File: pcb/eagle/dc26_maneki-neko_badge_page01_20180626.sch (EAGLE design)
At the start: 55 parts, among them T1 RK7002BMT116, U1 STM32F030C8T, U2 PAM2301CAAB330, U3 NPTC042KFMS-RC, U4 MIC2005A-1YM5-TR, U5 MIC2005A-1YM5-TR, U6 MIC2005A-1YM5-TR

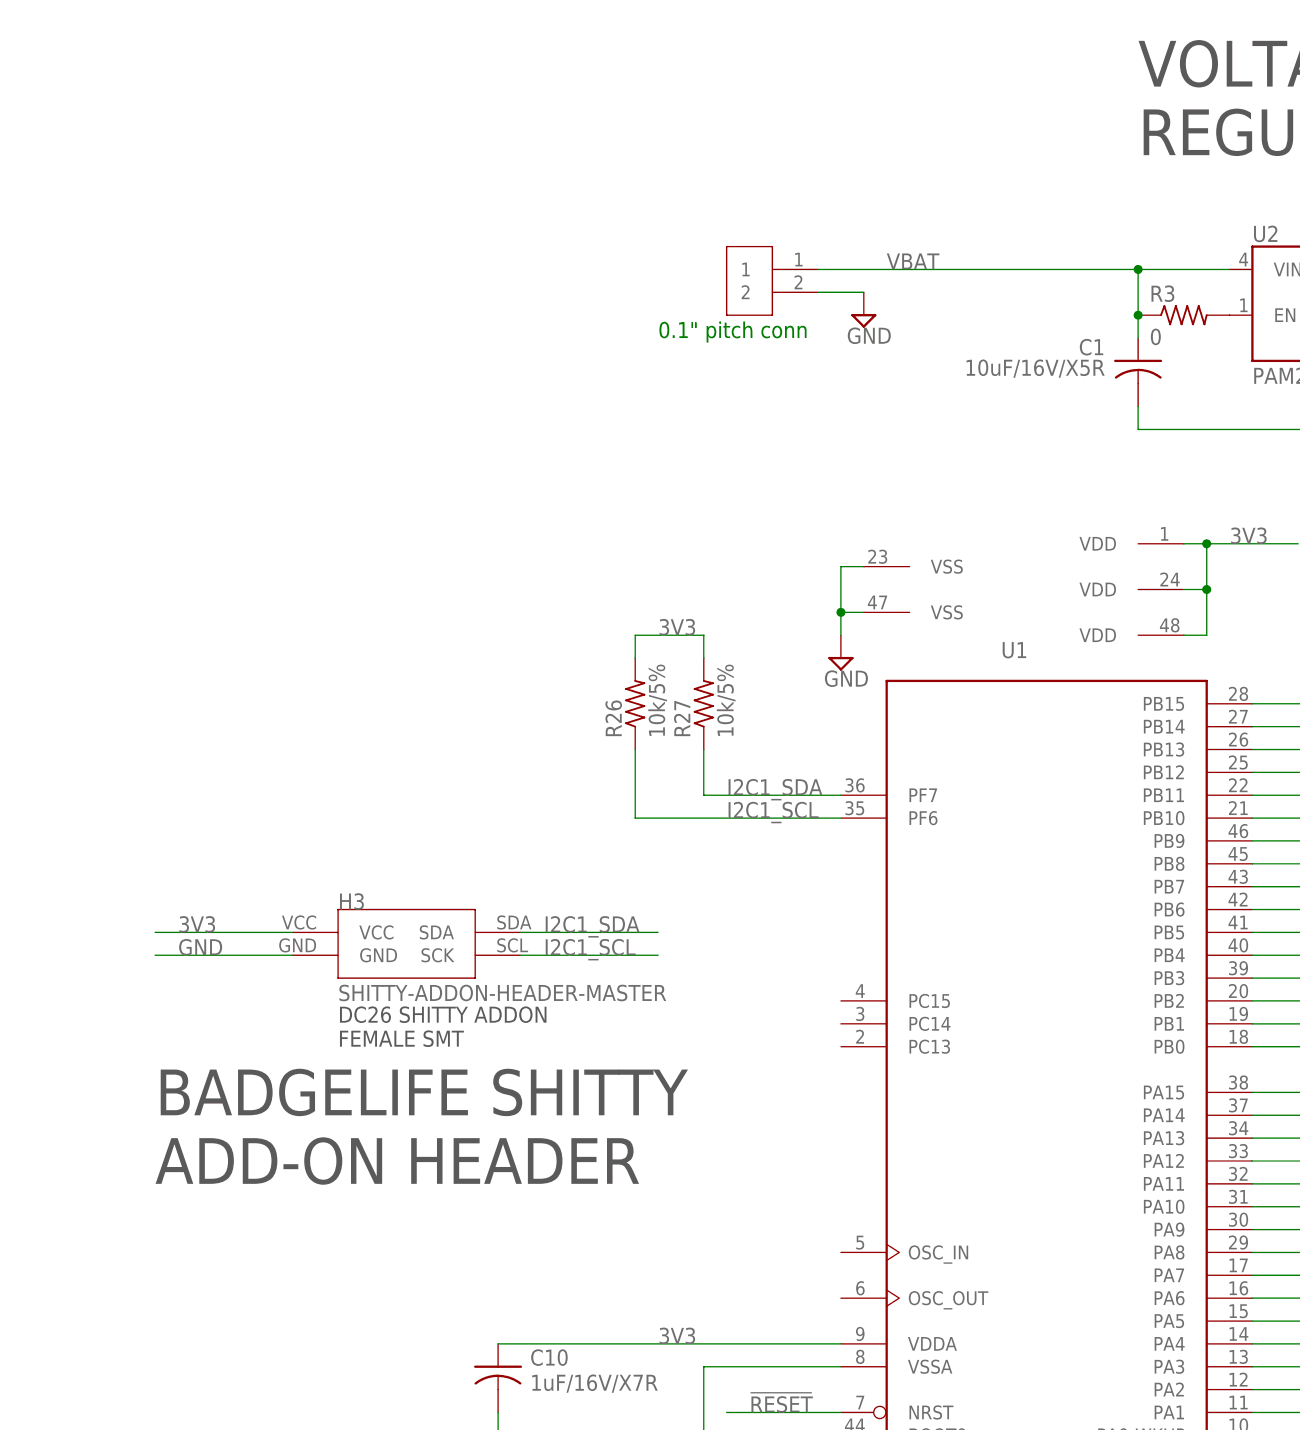
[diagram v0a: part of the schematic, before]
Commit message: added power switch and user button
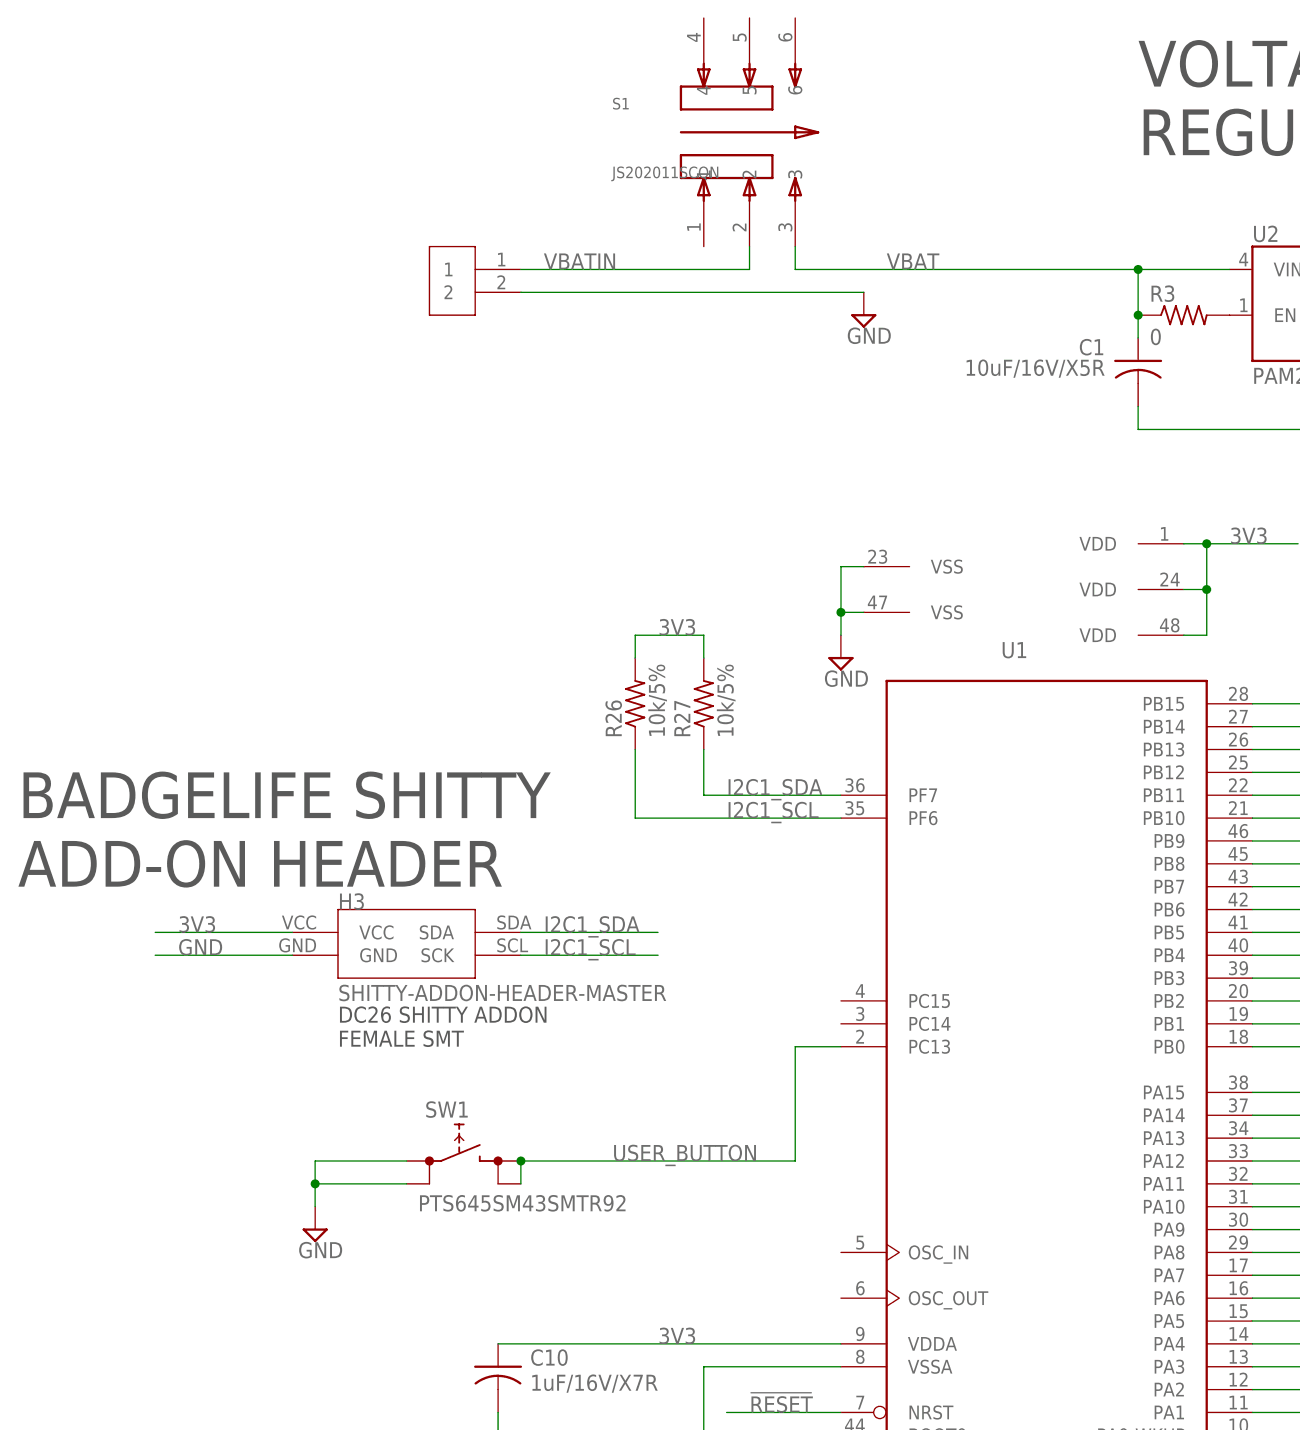
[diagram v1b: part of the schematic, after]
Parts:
- removed U$1: BATTPADS-SMT, battery_pads:BATTPADS-SMT
- added S1: JS202011SCQN, JS202011SCQN:JS202011SCQN
- added SW1: PTS645SM43SMTR92, PTS645SM43SMTR92:PTS645SM43SMTR92
- added U$2: BATTPADS-SMT, battery_pads:BATTPADS-SMT
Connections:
- new net USER_BUTTON: SW1.1@A, SW1.1@B, U1MCU.PC13
- new net VBATIN: S1.2, U$2.1
- net GND: now also SW1.0@A, SW1.0@B, U$2.2; no longer U$1.2
- net VBAT: now also S1.3; no longer U$1.1
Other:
- note removed: "0.1" pitch conn"
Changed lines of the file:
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@@
 <part name="SUPPLY19" library="supply2" library_urn="urn:adsk.eagle:library:372" deviceset="GND" device=""/>
 <part name="SUPPLY20" library="supply2" library_urn="urn:adsk.eagle:library:372" deviceset="GND" device=""/>
-<part name="U$1" library="battery_pads" deviceset="BATTPADS-SMT" device=""/>
 <part name="H2" library="M20-8890345R" deviceset="M20-8890345R" device=""/>
+<part name="SUPPLY21" library="supply2" library_urn="urn:adsk.eagle:library:372" deviceset="GND" device=""/>
+<part name="SW1" library="PTS645SM43SMTR92" deviceset="PTS645SM43SMTR92" device=""/>
+<part name="S1" library="JS202011SCQN" deviceset="JS202011SCQN" device=""/>
+<part name="U$2" library="battery_pads" deviceset="BATTPADS-SMT" device=""/>
 </parts>
 <sheets>
 <sheet>
 <plain>
-<text x="-187.96" y="218.44" size="1.778" layer="91">0.1" pitch conn</text>
 <text x="167.64" y="119.38" size="5.08" layer="97">RIGHT EYE</text>
 <text x="60.96" y="119.38" size="5.08" layer="97">LEFT EYE</text>
@@
 <text x="-121.92" y="40.64" size="5.08" layer="97">PGM/DEBUG
 HEADER</text>
-<text x="-243.84" y="124.46" size="5.08" layer="97">BADGELIFE SHITTY
+<text x="-259.08" y="157.48" size="5.08" layer="97">BADGELIFE SHITTY
 ADD-ON HEADER</text>
 <text x="-134.62" y="238.76" size="5.08" layer="97">VOLTAGE
@@
 <instance part="SUPPLY19" gate="GND" x="-167.64" y="182.88"/>
 <instance part="SUPPLY20" gate="GND" x="-96.52" y="185.42"/>
-<instance part="U$1" gate="G$1" x="-175.26" y="226.06" rot="MR0"/>
 <instance part="H2" gate="G$1" x="198.12" y="78.74"/>
+<instance part="SUPPLY21" gate="GND" x="-226.06" y="119.38"/>
+<instance part="SW1" gate="G$1" x="-210.82" y="127"/>
+<instance part="S1" gate="G$1" x="-177.8" y="241.3"/>
+<instance part="U$2" gate="G$1" x="-208.28" y="226.06" rot="MR0"/>
 </instances>
 <busses>
@@
 <segment>
 <pinref part="SUPPLY1" gate="GND" pin="GND"/>
-<wire x1="-170.18" y1="223.52" x2="-165.1" y2="223.52" width="0.1524" layer="91"/>
-<pinref part="U$1" gate="G$1" pin="2"/>
+<pinref part="U$2" gate="G$1" pin="2"/>
+<wire x1="-203.2" y1="223.52" x2="-165.1" y2="223.52" width="0.1524" layer="91"/>
 </segment>
 <segment>
@@
 <junction x="-96.52" y="187.96"/>
 </segment>
+<segment>
+<pinref part="SW1" gate="G$1" pin="0@B"/>
+<pinref part="SUPPLY21" gate="GND" pin="GND"/>
+<wire x1="-215.9" y1="124.46" x2="-226.06" y2="124.46" width="0.1524" layer="91"/>
+<wire x1="-226.06" y1="124.46" x2="-226.06" y2="121.92" width="0.1524" layer="91"/>
+<pinref part="SW1" gate="G$1" pin="0@A"/>
+<wire x1="-215.9" y1="127" x2="-226.06" y2="127" width="0.1524" layer="91"/>
+<wire x1="-226.06" y1="127" x2="-226.06" y2="124.46" width="0.1524" layer="91"/>
+<junction x="-226.06" y="124.46"/>
+</segment>
 </net>
 <net name="VBAT" class="0">
@@
 <wire x1="-124.46" y1="226.06" x2="-134.62" y2="226.06" width="0.1524" layer="91"/>
 <junction x="-134.62" y="226.06"/>
-<wire x1="-134.62" y1="226.06" x2="-170.18" y2="226.06" width="0.1524" layer="91"/>
+<wire x1="-134.62" y1="226.06" x2="-172.72" y2="226.06" width="0.1524" layer="91"/>
 <pinref part="R3" gate="G$1" pin="1"/>
 <junction x="-134.62" y="220.98"/>
 <pinref part="U2" gate="G$1" pin="VIN"/>
-<pinref part="U$1" gate="G$1" pin="1"/>
+<pinref part="S1" gate="G$1" pin="3"/>
+<wire x1="-172.72" y1="226.06" x2="-172.72" y2="228.6" width="0.1524" layer="91"/>
 </segment>
 <segment>
@@
 </segment>
 </net>
+<net name="USER_BUTTON" class="0">
+<segment>
+<pinref part="U1" gate="MCU" pin="PC13"/>
+<wire x1="-167.64" y1="139.7" x2="-172.72" y2="139.7" width="0.1524" layer="91"/>
+<wire x1="-172.72" y1="139.7" x2="-172.72" y2="127" width="0.1524" layer="91"/>
+<wire x1="-172.72" y1="127" x2="-203.2" y2="127" width="0.1524" layer="91"/>
+<label x="-193.04" y="127" size="1.778" layer="95"/>
+<pinref part="SW1" gate="G$1" pin="1@A"/>
+<pinref part="SW1" gate="G$1" pin="1@B"/>
+<wire x1="-203.2" y1="124.46" x2="-203.2" y2="127" width="0.1524" layer="91"/>
+<junction x="-203.2" y="127"/>
+</segment>
+</net>
+<net name="VBATIN" class="0">
+<segment>
+<pinref part="U$2" gate="G$1" pin="1"/>
+<wire x1="-203.2" y1="226.06" x2="-177.8" y2="226.06" width="0.1524" layer="91"/>
+<pinref part="S1" gate="G$1" pin="2"/>
+<wire x1="-177.8" y1="226.06" x2="-177.8" y2="228.6" width="0.1524" layer="91"/>
+<label x="-200.66" y="226.06" size="1.778" layer="95"/>
+</segment>
+</net>

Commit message: OUT TO FAB OMG 2560256025602560
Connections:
- net !RESET: now also H1.9; no longer H1.10
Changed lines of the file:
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@@
 <net name="!RESET" class="0">
-<segment>
-<pinref part="H1" gate="G$1" pin="10"/>
-<wire x1="-93.98" y1="63.5" x2="-68.58" y2="63.5" width="0.1524" layer="91"/>
-<label x="-88.9" y="63.5" size="1.778" layer="95"/>
-</segment>
 <segment>
 <pinref part="U1" gate="MCU" pin="NRST"/>
@@
 <label x="-177.8" y="99.06" size="1.778" layer="95"/>
 </segment>
+<segment>
+<wire x1="-114.3" y1="63.5" x2="-129.54" y2="63.5" width="0.1524" layer="91"/>
+<label x="-119.38" y="63.5" size="1.778" layer="95" rot="MR0"/>
+<pinref part="H1" gate="G$1" pin="9"/>
+</segment>
 </net>
